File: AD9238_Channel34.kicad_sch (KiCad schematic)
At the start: 55 parts, among them J4 BWSMA-KE-P001, J5 BWSMA-KE-P001, U14 AD8065, U15 AD8065, U16 AD8138, U17 AD8138, U18 AD9238

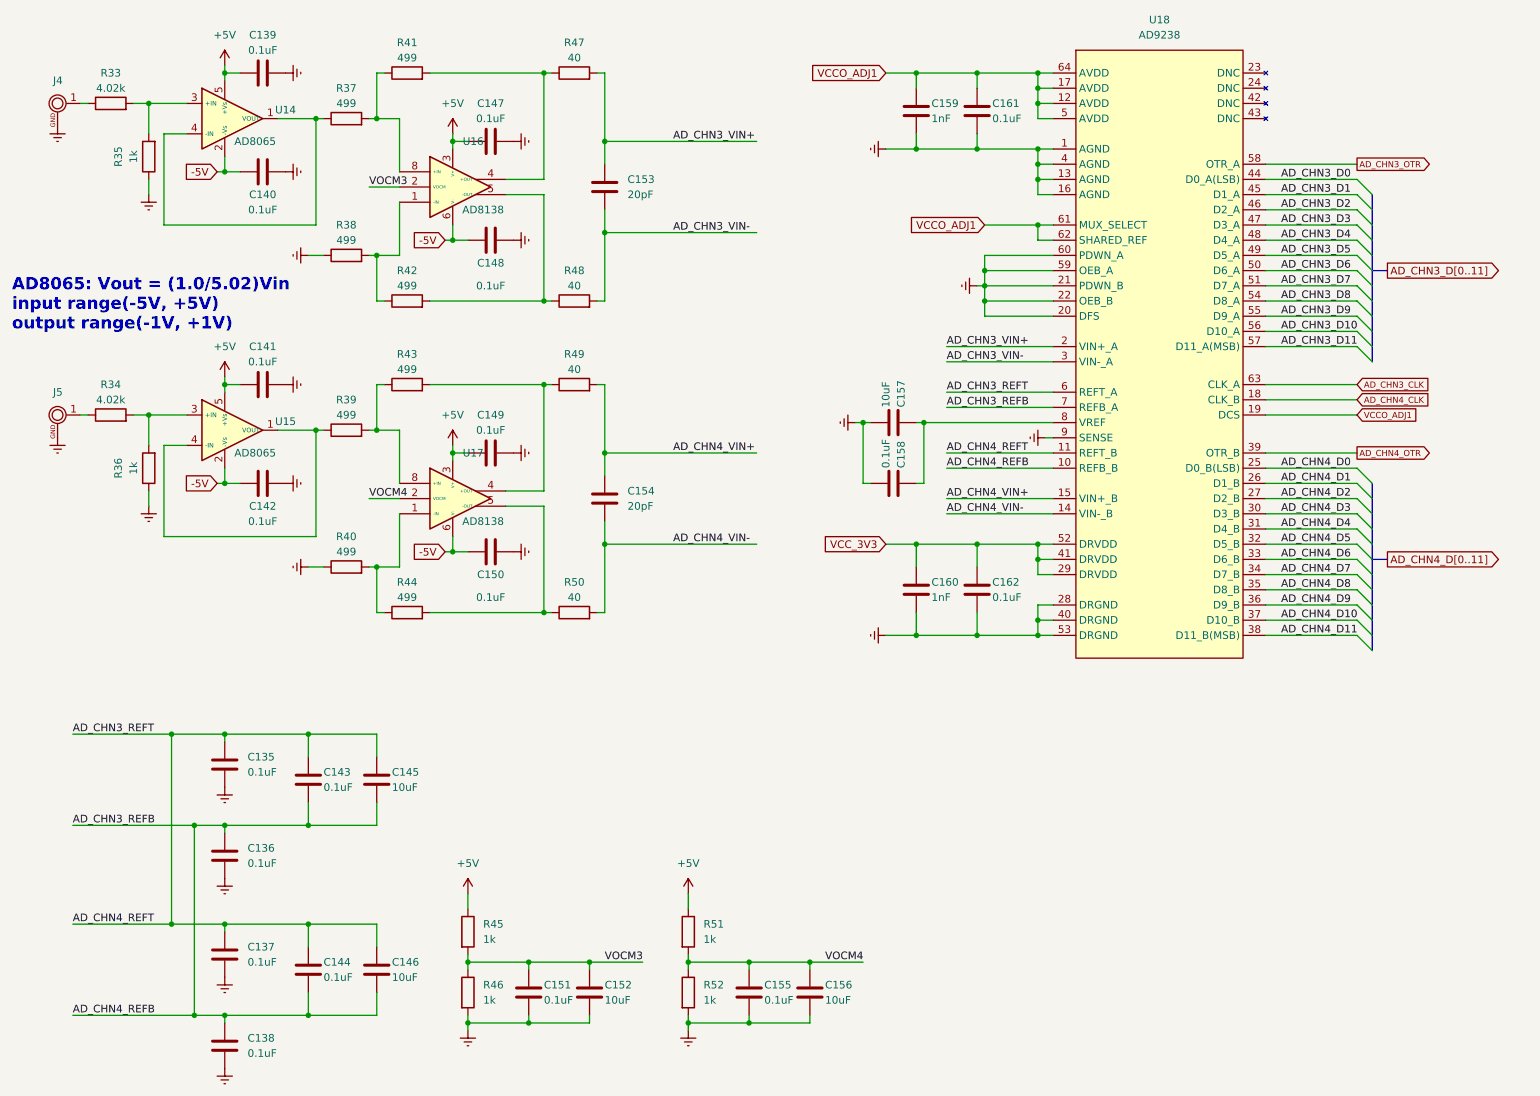
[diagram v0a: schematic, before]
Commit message: 变压器输入+两块DDR3
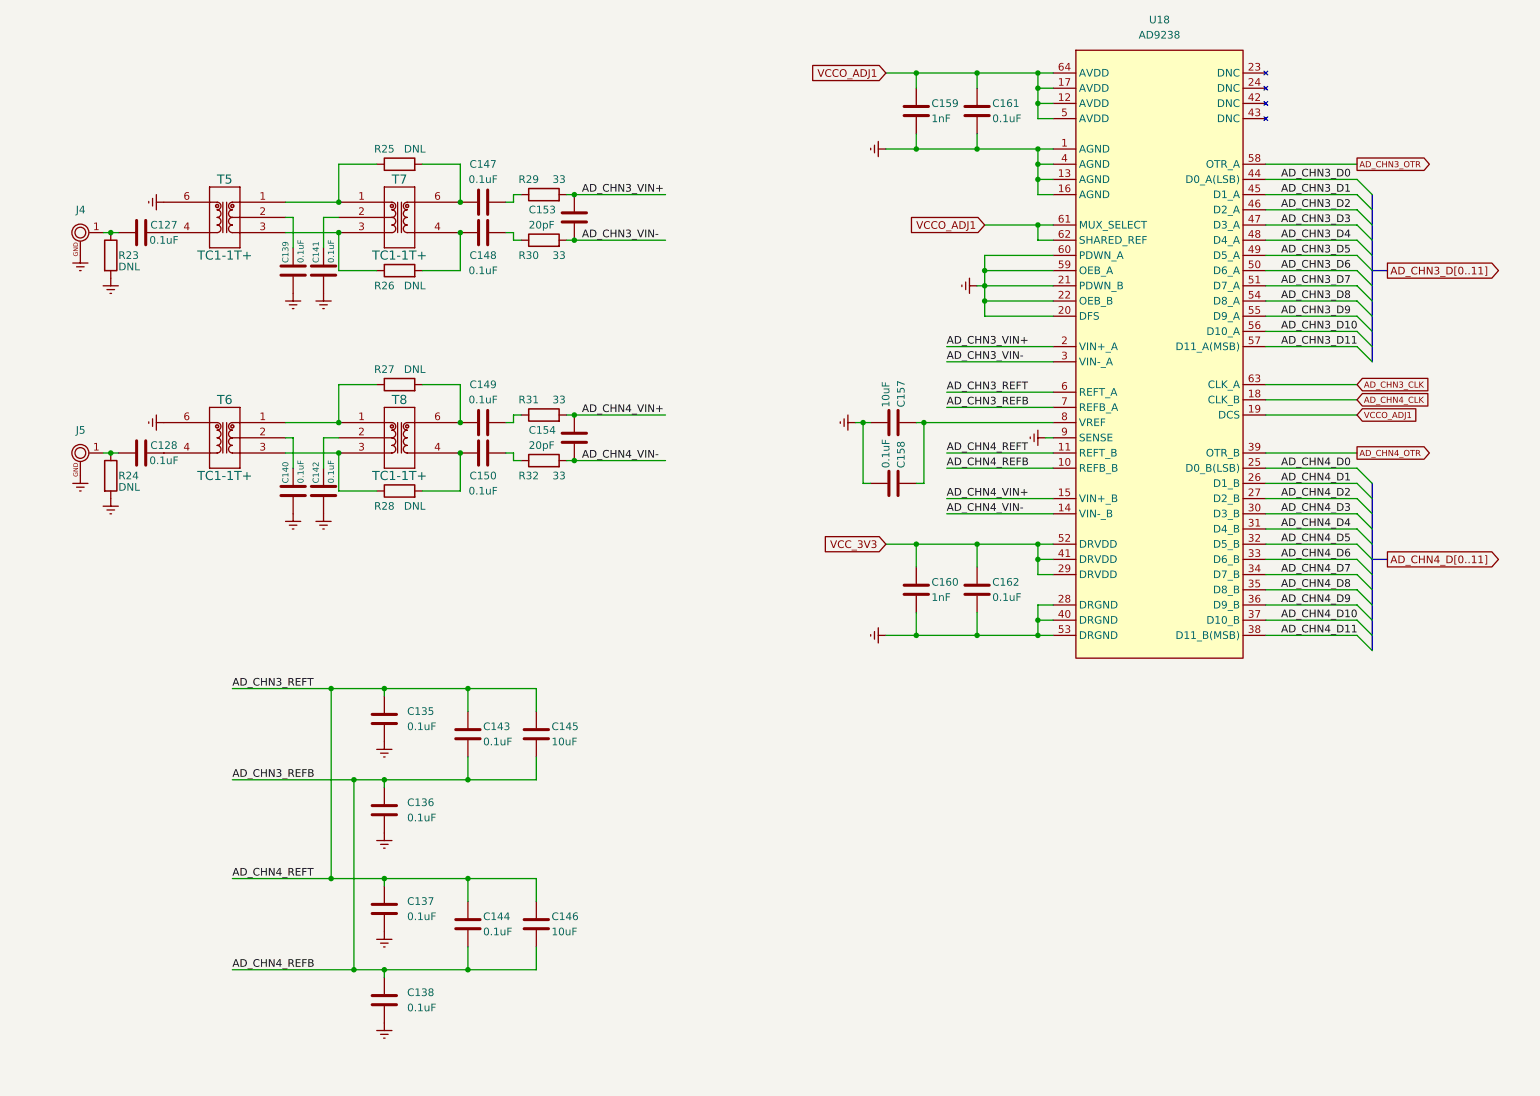
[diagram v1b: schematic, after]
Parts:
- removed C151, C155: 0.1uF, Capacitor_SMD:C_0402_1005Metric, symbol Device:C
- removed C152, C156: 10uF, Capacitor_SMD:C_0603_1608Metric, symbol Device:C
- removed R33, R34: 4.02k, Resistor_SMD:R_0402_1005Metric, symbol Device:R
- removed R35, R36, R45, R46, R51, R52: 1k, Resistor_SMD:R_0402_1005Metric, symbol Device:R
- removed R37, R38, R39, R40, R41, R42, R43, R44: 499, Resistor_SMD:R_0402_1005Metric, symbol Device:R
- removed R47, R48, R49, R50: 40, Resistor_SMD:R_0402_1005Metric, symbol Device:R
- removed U14, U15: AD8065, Package_TO_SOT_SMD:SOT-23-5, symbol Zynq7020_AD9238:AD8065
- removed U16, U17: AD8138, Package_SO:SOIC-8_3.9x4.9mm_P1.27mm, symbol Zynq7020_AD9238:AD8138
- added C127, C128: 0.1uF, Capacitor_SMD:C_0402_1005Metric, symbol Device:C
- added R23, R24, R25, R26, R27, R28: DNL, Resistor_SMD:R_0402_1005Metric, symbol Device:R
- added R29, R30, R31, R32: 33, Resistor_SMD:R_0402_1005Metric, symbol Device:R
- added T5, T6, T7, T8: TC1-1T+, Transformer_SMD:Transformer_MiniCircuits_AT224-1A, symbol Zynq7020_AD9238:TC1-1T+
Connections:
- net AD_CHN3_VIN+: now also C153.1, R29.2; no longer C153.2
- net AD_CHN3_VIN-: now also C153.2, R30.2; no longer C153.1
- net AD_CHN4_VIN+: now also C154.1, R31.2; no longer C154.2
- net AD_CHN4_VIN-: now also C154.2, R32.2; no longer C154.1
- net Earth: now also C139.1, C140.1, C141.1, C142.1, R23.2, R24.2, T5.6, T6.6; no longer C139.2, C140.2, C141.2, C142.2, C147.2, C148.2, C149.2, C150.2
- net at J4.1 (IN): now also C127.1, R23.1
- net at J5.1 (IN): now also C128.1, R24.1
- removed net +5V: C139.1, C141.1, C147.1, C149.1
- removed net -5V: C140.1, C142.1, C148.1, C150.1
- new net: R27.1, T6.1, T8.1
- new net: C149.1, R27.2, T8.6
- new net: C139.2, T5.2
- new net: C127.2, T5.4
- new net: C147.1, R25.2, T7.6
- new net: C147.2, R29.1
- new net: C128.2, T6.4
- new net: C148.1, R26.2, T7.4
- new net: C148.2, R30.1
- new net: C141.2, T7.2
- new net: C142.2, T8.2
- new net: R28.1, T6.3, T8.3
- new net: C150.1, R28.2, T8.4
- new net: C149.2, R31.1
- new net: R25.1, T5.1, T7.1
- new net: R26.1, T5.3, T7.3
- new net: C140.2, T6.2
- new net: C150.2, R32.1
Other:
- note removed: "AD8065: Vout = (1.0/5.02)Vin input range(-5V, +5V) output range(-1V, +1V)"
- moved on the sheet: C135, C136, C137, C138, C143, C144, C145, C146

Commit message: 删除-5V电源，添加eMMC模块接口
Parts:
- renumbered C127 to C133, C128 to C134, C139 to C135, C140 to C136, C141 to C137, C142 to C138, C135 to C139, C136 to C140, C137 to C141, C138 to C142, C147 to C145, C148 to C146, C149 to C147, C150 to C148, C145 to C149, C146 to C150, C153 to C151, C154 to C152, C157 to C153, C158 to C154, C159 to C155, C160 to C156, C161 to C157, C162 to C158, U18 to U10
